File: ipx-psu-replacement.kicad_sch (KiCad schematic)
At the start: 29 parts, among them J1 L, J10 -12V, J11 GND, J12 Fan, J13 SENS, J14 GND, J15 GND, J2 AC IN, J3 GND, J4 Floppy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

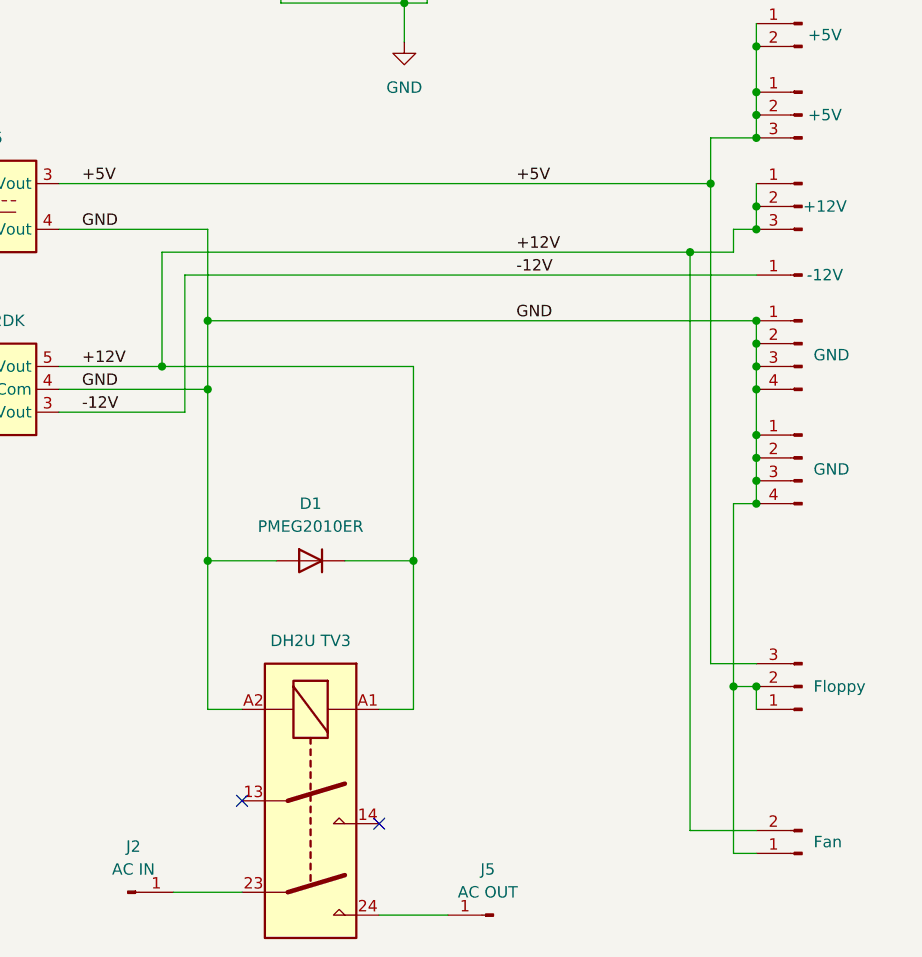
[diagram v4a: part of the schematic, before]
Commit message: add base load resistors
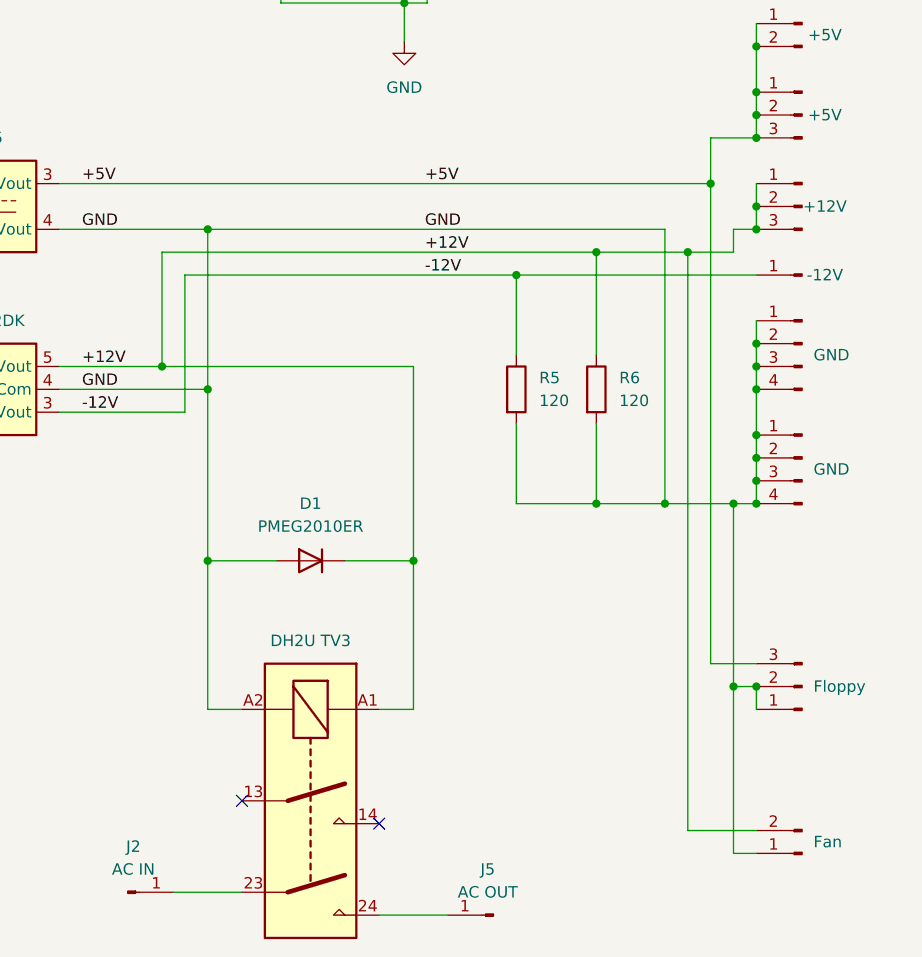
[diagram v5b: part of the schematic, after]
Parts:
- added R5, R6: 120, Resistor_THT:R_Axial_DIN0922_L20.0mm_D9.0mm_P25.40mm_Horizontal, symbol Device:R
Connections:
- net +12V: now also R6.1
- net -12V: now also R5.1
- net GND: now also R5.2, R6.2
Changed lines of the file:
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@@
   (junction (at 189.23 82.55) (diameter 0) (color 0 0 0 0)
   )
-  (junction (at 186.944 90.17) (diameter 0) (color 0 0 0 0)
-  )
   (junction (at 155.194 62.484) (diameter 0) (color 0 0 0 0)
   )
@@
   (junction (at 194.31 87.63) (diameter 0) (color 0 0 0 0)
   )
+  (junction (at 133.35 87.63) (diameter 0) (color 0 0 0 0)
+  )
   (junction (at 245.872 70.104) (diameter 0) (color 0 0 0 0)
   )
+  (junction (at 186.69 90.17) (diameter 0) (color 0 0 0 0)
+  )
   (junction (at 194.31 105.41) (diameter 0) (color 0 0 0 0)
   )
@@
   (junction (at 67.31 107.95) (diameter 0) (color 0 0 0 0)
   )
-  (junction (at 133.35 97.79) (diameter 0) (color 0 0 0 0)
-  )
   (junction (at 141.478 55.372) (diameter 0) (color 0 0 0 0)
   )
+  (junction (at 167.64 92.71) (diameter 0) (color 0 0 0 0)
+  )
   (junction (at 157.734 21.844) (diameter 0) (color 0 0 0 0)
   )
-  (junction (at 194.31 97.79) (diameter 0) (color 0 0 0 0)
+  (junction (at 176.53 90.17) (diameter 0) (color 0 0 0 0)
   )
   (junction (at 194.31 85.09) (diameter 0) (color 0 0 0 0)
@@
   (junction (at 194.31 115.57) (diameter 0) (color 0 0 0 0)
   )
+  (junction (at 184.15 118.11) (diameter 0) (color 0 0 0 0)
+  )
   (junction (at 194.31 74.93) (diameter 0) (color 0 0 0 0)
   )
@@
   (junction (at 128.27 102.87) (diameter 0) (color 0 0 0 0)
   )
+  (junction (at 176.53 118.11) (diameter 0) (color 0 0 0 0)
+  )
   (junction (at 191.77 138.43) (diameter 0) (color 0 0 0 0)
   )
@@
   )
   (junction (at 105.918 40.386) (diameter 0) (color 0 0 0 0)
+  )
+  (junction (at 191.77 118.11) (diameter 0) (color 0 0 0 0)
   )
   (junction (at 156.21 124.46) (diameter 0) (color 0 0 0 0)
@@
   (no_connect (at 155.194 24.892))
   (no_connect (at 121.158 37.846))
+  (wire (pts (xy 167.64 92.71) (xy 167.64 101.6))
+    (stroke (width 0) (type default))
+  )
   (wire (pts (xy 38.862 53.34) (xy 38.862 43.18))
     (stroke (width 0) (type default))
@@
     (stroke (width 0) (type default))
   )
-  (wire (pts (xy 186.944 90.17) (xy 186.944 154.432))
+  (wire (pts (xy 186.69 90.17) (xy 186.69 154.432))
     (stroke (width 0) (type default))
   )
@@
     (stroke (width 0) (type default))
   )
-  (wire (pts (xy 133.35 87.63) (xy 133.35 97.79))
-    (stroke (width 0) (type default))
-  )
   (wire (pts (xy 194.31 138.43) (xy 194.31 140.97))
     (stroke (width 0) (type default))
@@
     (stroke (width 0) (type default))
   )
+  (wire (pts (xy 176.53 90.17) (xy 176.53 101.6))
+    (stroke (width 0) (type default))
+  )
   (wire (pts (xy 55.626 27.94) (xy 61.722 27.94))
     (stroke (width 0) (type default))
@@
     (stroke (width 0) (type default))
   )
+  (wire (pts (xy 184.15 87.63) (xy 184.15 118.11))
+    (stroke (width 0) (type default))
+  )
   (wire (pts (xy 142.494 45.212) (xy 141.478 45.212))
     (stroke (width 0) (type default))
@@
     (stroke (width 0) (type default))
   )
-  (wire (pts (xy 186.944 90.17) (xy 191.77 90.17))
+  (wire (pts (xy 186.69 90.17) (xy 191.77 90.17))
     (stroke (width 0) (type default))
   )
@@
     (stroke (width 0) (type default))
   )
-  (wire (pts (xy 128.27 90.17) (xy 186.944 90.17))
-    (stroke (width 0) (type default))
-  )
   (wire (pts (xy 173.736 29.718) (xy 173.736 35.052))
     (stroke (width 0) (type default))
@@
     (stroke (width 0) (type default))
   )
-  (wire (pts (xy 130.81 92.71) (xy 194.31 92.71))
+  (wire (pts (xy 130.81 92.71) (xy 167.64 92.71))
+    (stroke (width 0) (type default))
+  )
+  (wire (pts (xy 176.53 90.17) (xy 186.69 90.17))
     (stroke (width 0) (type default))
   )
@@
     (stroke (width 0) (type default))
   )
+  (wire (pts (xy 167.64 92.71) (xy 194.31 92.71))
+    (stroke (width 0) (type default))
+  )
   (wire (pts (xy 128.27 90.17) (xy 128.27 102.87))
     (stroke (width 0) (type default))
@@
     (stroke (width 0) (type default))
   )
+  (wire (pts (xy 128.27 90.17) (xy 176.53 90.17))
+    (stroke (width 0) (type default))
+  )
+  (wire (pts (xy 176.53 109.22) (xy 176.53 118.11))
+    (stroke (width 0) (type default))
+  )
   (wire (pts (xy 116.84 82.55) (xy 189.23 82.55))
     (stroke (width 0) (type default))
@@
     (stroke (width 0) (type default))
   )
-  (wire (pts (xy 194.31 154.432) (xy 186.944 154.432))
+  (wire (pts (xy 176.53 118.11) (xy 184.15 118.11))
+    (stroke (width 0) (type default))
+  )
+  (wire (pts (xy 194.31 154.432) (xy 186.69 154.432))
     (stroke (width 0) (type default))
   )
@@
     (stroke (width 0) (type default))
   )
-  (wire (pts (xy 133.35 97.79) (xy 194.31 97.79))
+  (wire (pts (xy 184.15 118.11) (xy 191.77 118.11))
     (stroke (width 0) (type default))
   )
@@
     (stroke (width 0) (type default))
   )
+  (wire (pts (xy 167.64 109.22) (xy 167.64 118.11))
+    (stroke (width 0) (type default))
+  )
   (wire (pts (xy 155.194 62.484) (xy 155.194 66.802))
     (stroke (width 0) (type default))
@@
     (stroke (width 0) (type default))
   )
+  (wire (pts (xy 167.64 118.11) (xy 176.53 118.11))
+    (stroke (width 0) (type default))
+  )
   (wire (pts (xy 62.23 82.55) (xy 96.52 82.55))
     (stroke (width 0) (type default))
@@
     (stroke (width 0) (type default))
   )
+  (wire (pts (xy 133.35 87.63) (xy 184.15 87.63))
+    (stroke (width 0) (type default))
+  )
   (wire (pts (xy 67.31 107.95) (xy 96.52 107.95))
     (stroke (width 0) (type default))
@@
     (stroke (width 0) (type default))
   )
-  (wire (pts (xy 133.35 97.79) (xy 133.35 105.41))
+  (wire (pts (xy 133.35 87.63) (xy 133.35 105.41))
     (stroke (width 0) (type default))
   )
@@
     (effects (font (size 1.27 1.27)) (justify left bottom))
   )
-  (label "-12V" (at 167.64 92.71 0) (fields_autoplaced)
+  (label "-12V" (at 157.48 92.71 0) (fields_autoplaced)
     (effects (font (size 1.27 1.27)) (justify left bottom))
   )
@@
     (effects (font (size 1.27 1.27)) (justify left bottom))
   )
-  (label "+12V" (at 167.64 90.17 0) (fields_autoplaced)
-    (effects (font (size 1.27 1.27)) (justify left bottom))
-  )
-  (label "+5V" (at 167.64 82.55 0) (fields_autoplaced)
+  (label "+12V" (at 157.48 90.17 0) (fields_autoplaced)
+    (effects (font (size 1.27 1.27)) (justify left bottom))
+  )
+  (label "+5V" (at 157.48 82.55 0) (fields_autoplaced)
     (effects (font (size 1.27 1.27)) (justify left bottom))
   )
@@
     (effects (font (size 1.27 1.27)) (justify left bottom))
   )
-  (label "GND" (at 167.64 97.79 0) (fields_autoplaced)
+  (label "GND" (at 157.48 87.63 0) (fields_autoplaced)
     (effects (font (size 1.27 1.27)) (justify left bottom))
   )
@@
     )
   )
+  (symbol (lib_id "Device:R") (at 167.64 105.41 0) (unit 1)
+    (in_bom yes) (on_board yes) (dnp no) (fields_autoplaced)
+    (property "Reference" "R5" (at 170.18 104.14 0)
+      (effects (font (size 1.27 1.27)) (justify left))
+    )
+    (property "Value" "120" (at 170.18 106.68 0)
+      (effects (font (size 1.27 1.27)) (justify left))
+    )
+    (property "Footprint" "Resistor_THT:R_Axial_DIN0922_L20.0mm_D9.0mm_P25.40mm_Horizontal" (at 165.862 105.41 90)
+      (effects (font (size 1.27 1.27)) hide)
+    )
+    (property "Datasheet" "~" (at 167.64 105.41 0)
+      (effects (font (size 1.27 1.27)) hide)
+    )
+    (pin "1")
+    (pin "2")
+    (instances
+      (project "ipx-psu-replacement"
+        (path "/80e599cc-36ff-4f54-a2a4-590742b133b5"
+          (reference "R5") (unit 1)
+        )
+      )
+    )
+  )
   (symbol (lib_id "Device:R_Small") (at 195.834 27.178 0) (unit 1)
     (in_bom yes) (on_board yes) (dnp no)
@@
         )
       )
+    )
+  )
+  (symbol (lib_id "Device:R") (at 176.53 105.41 0) (unit 1)
+    (in_bom yes) (on_board yes) (dnp no) (fields_autoplaced)
+    (property "Reference" "R6" (at 179.07 104.14 0)
+      (effects (font (size 1.27 1.27)) (justify left))
+    )
+    (property "Value" "120" (at 179.07 106.68 0)
+      (effects (font (size 1.27 1.27)) (justify left))
+    )
+    (property "Footprint" "Resistor_THT:R_Axial_DIN0922_L20.0mm_D9.0mm_P25.40mm_Horizontal" (at 174.752 105.41 90)
+      (effects (font (size 1.27 1.27)) hide)
+    )
+    (property "Datasheet" "~" (at 176.53 105.41 0)
+      (effects (font (size 1.27 1.27)) hide)
+    )
+    (pin "1")
+    (pin "2")
+    (instances
+      (project "ipx-psu-replacement"
+        (path "/80e599cc-36ff-4f54-a2a4-590742b133b5"
+          (reference "R6") (unit 1)
+        )
+      )

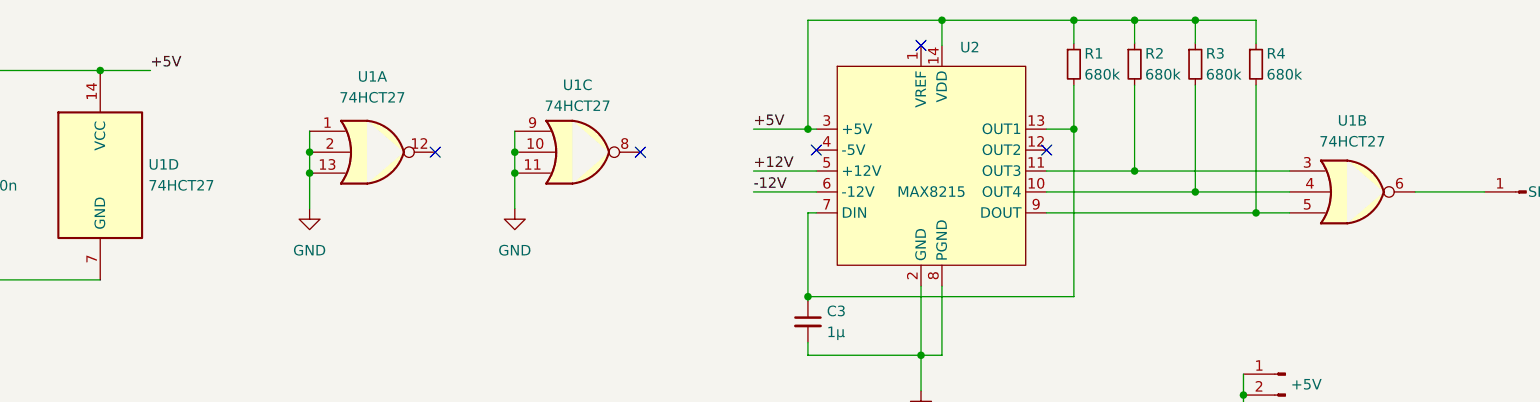
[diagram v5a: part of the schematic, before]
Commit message: hct27 -> hct11
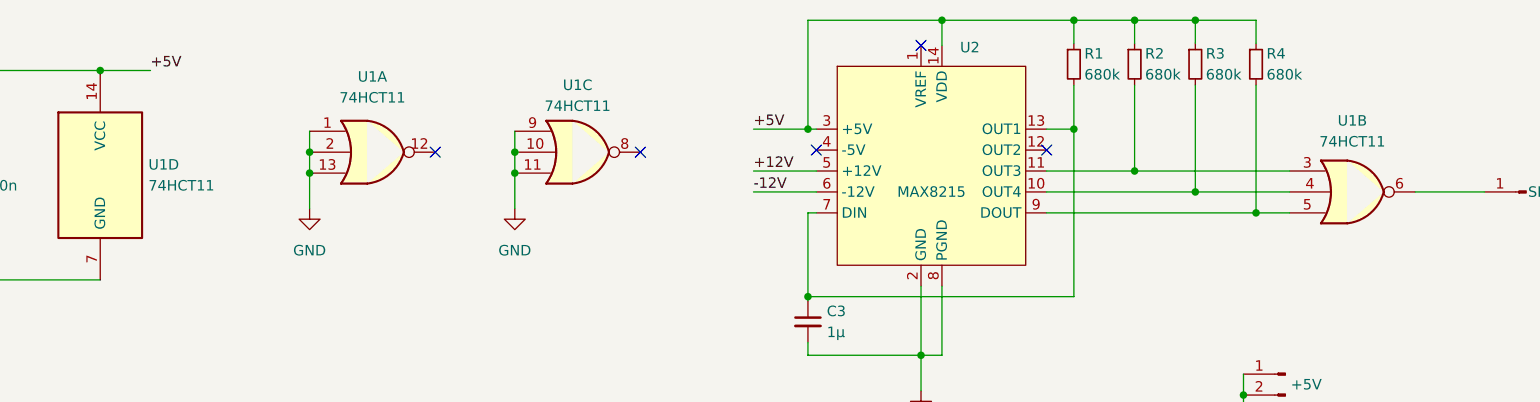
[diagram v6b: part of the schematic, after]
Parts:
- U1: value 74HCT27 -> 74HCT11
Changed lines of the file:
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@@
       (effects (font (size 1.27 1.27)))
     )
-    (property "Value" "74HCT27" (at 113.538 32.258 0)
+    (property "Value" "74HCT11" (at 113.538 32.258 0)
       (effects (font (size 1.27 1.27)))
     )
@@
       (effects (font (size 1.27 1.27)) hide)
     )
-    (property "Datasheet" "http://www.ti.com/lit/gpn/sn74LS27" (at 113.538 37.846 0)
+    (property "Datasheet" "http://www.ti.com/lit/gpn/sn74LS11" (at 113.538 37.846 0)
       (effects (font (size 1.27 1.27)) hide)
     )
@@
       (effects (font (size 1.27 1.27)) (justify left))
     )
-    (property "Value" "74HCT27" (at 61.468 41.91 0)
+    (property "Value" "74HCT11" (at 61.468 41.91 0)
       (effects (font (size 1.27 1.27)) (justify left))
     )
@@
       (effects (font (size 1.27 1.27)) hide)
     )
-    (property "Datasheet" "http://www.ti.com/lit/gpn/sn74LS27" (at 55.626 40.64 0)
+    (property "Datasheet" "http://www.ti.com/lit/gpn/sn74LS11" (at 55.626 40.64 0)
       (effects (font (size 1.27 1.27)) hide)
     )
@@
       (effects (font (size 1.27 1.27)))
     )
-    (property "Value" "74HCT27" (at 207.518 36.576 0)
+    (property "Value" "74HCT11" (at 207.518 36.576 0)
       (effects (font (size 1.27 1.27)))
     )
@@
       (effects (font (size 1.27 1.27)) hide)
     )
-    (property "Datasheet" "http://www.ti.com/lit/gpn/sn74LS27" (at 207.518 42.672 0)
+    (property "Datasheet" "http://www.ti.com/lit/gpn/sn74LS11" (at 207.518 42.672 0)
       (effects (font (size 1.27 1.27)) hide)
     )
@@
       (effects (font (size 1.27 1.27)))
     )
-    (property "Value" "74HCT27" (at 88.646 31.242 0)
+    (property "Value" "74HCT11" (at 88.646 31.242 0)
       (effects (font (size 1.27 1.27)))
     )
@@
       (effects (font (size 1.27 1.27)) hide)
     )
-    (property "Datasheet" "http://www.ti.com/lit/gpn/sn74LS27" (at 88.646 37.846 0)
-      (effects (font (size 1.27 1.27)) hide)
-    )
+    (property "Datasheet" "http://www.ti.com/lit/gpn/sn74LS11" (at 88.646 37.846 0)
+      (effects (font (size 1.27 1.27)) hide)
+    )
